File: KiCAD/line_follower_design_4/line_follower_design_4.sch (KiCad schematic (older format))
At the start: 50 parts

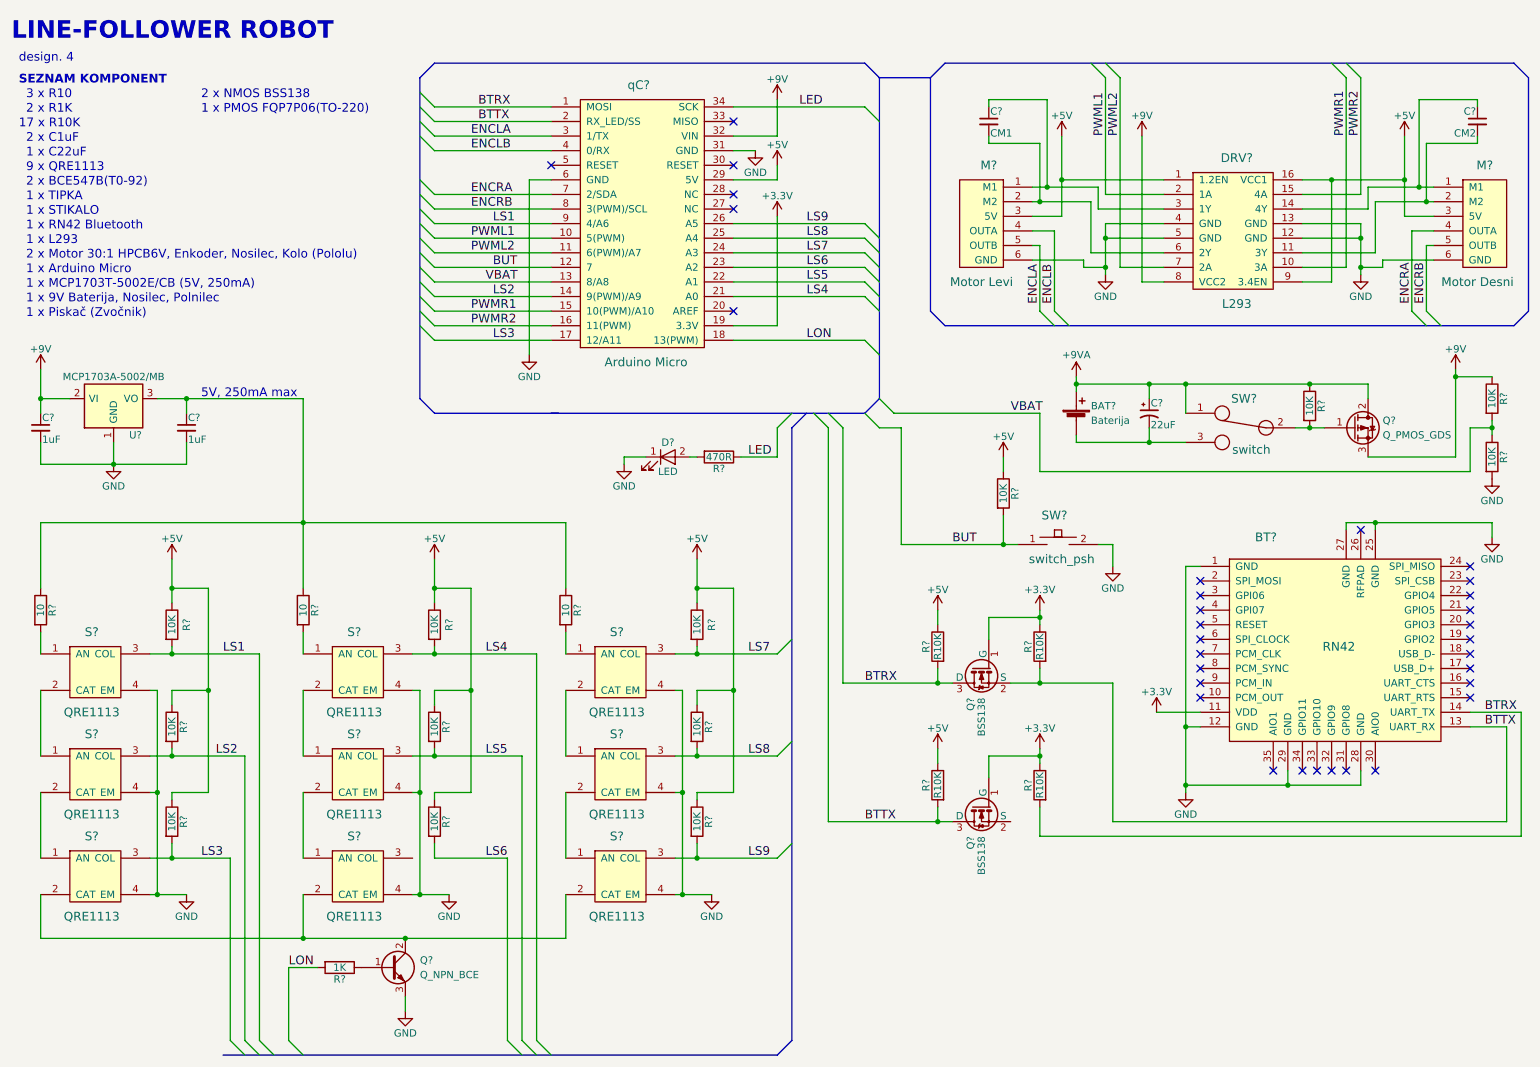
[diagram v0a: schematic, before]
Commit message: line-follower-design 4 updates
Shematic updates, library updates, netlist, unrouted PCB layout (1st
iteration).
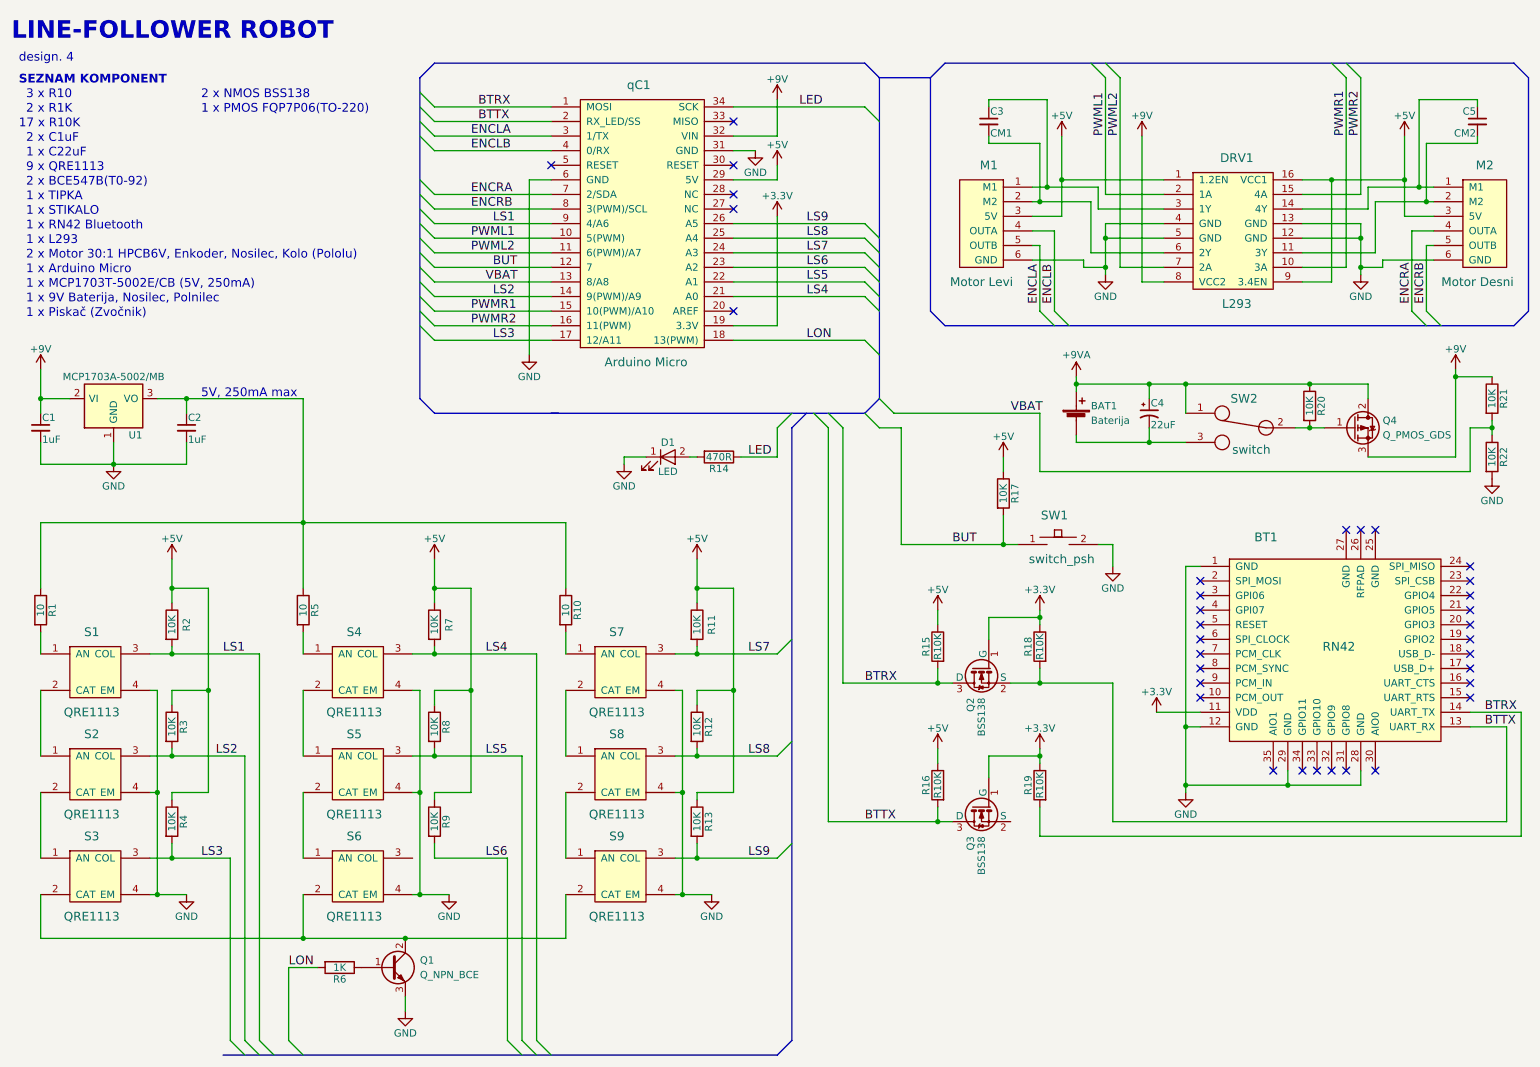
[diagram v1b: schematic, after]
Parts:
- BAT1: renamed from BAT?; footprint (none) -> 9VBattery_holder:12BH611-GR
- BT1: renamed from BT?; footprint (none) -> RF_Modules:RN42
- C1, C2, C3, C4, C5: renamed from C?; footprint (none) -> Capacitors_SMD:C_0603_HandSoldering
- D1: renamed from D?; footprint (none) -> LEDs:LED_D3.0mm_Horizontal_O1.27mm_Z2.0mm
- DRV1: renamed from DRV?; footprint (none) -> L293D:L293D
- M1, M2: renamed from M?; footprint (none) -> HPCBMotor:HPCB Motor (Pololu)
- Q1: renamed from Q?; footprint (none) -> Transistors_OldSowjetAera:OldSowjetaera_Transistor_Type-I_SmallPads
- Q4: renamed from Q?; footprint (none) -> TO_SOT_Packages_THT:TO-220_Horizontal
- R1, R10, R11, R12, R13, R14, R15, R16, R17, R18, R19, R2, R20, R21, R22, R3, R4, R5, R6, R7, R8, R9: renamed from R?; footprint (none) -> Resistors_SMD:R_1210_HandSoldering
- S1, S2, S3, S4, S5, S6, S7, S8, S9: renamed from S?; footprint (none) -> QRE1113:QRE1113
- SW1: renamed from SW?; footprint (none) -> Buttons_Switches_SMD:SW_SPST_EVQP0
- SW2: renamed from SW?; footprint (none) -> Buttons_Switches_SMD:SW_SPST_B3U-3100P
- gave numbers to parts that had none: 4
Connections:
- net GND: no longer BT1.25 (GND), BT1.27 (GND)
- no-connect marks 32 -> 34

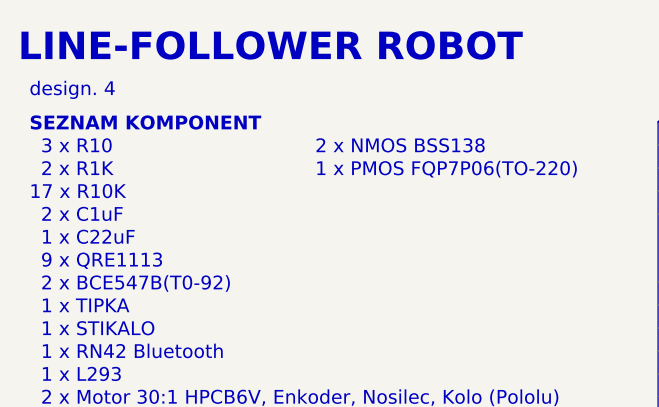
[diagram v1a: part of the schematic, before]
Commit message: line-follower-design-4 schematic update, pcb update
Library dependencies update, PCB components optimizations.
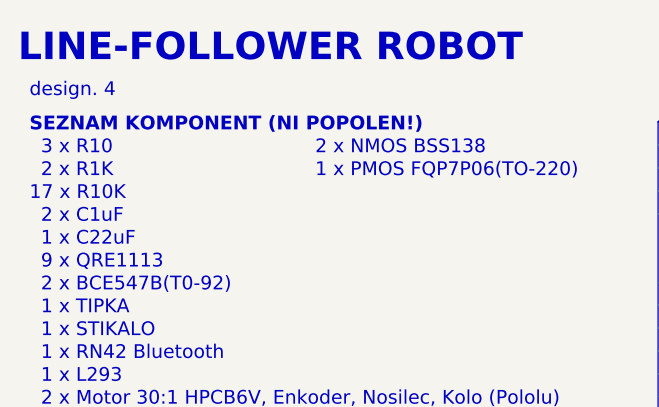
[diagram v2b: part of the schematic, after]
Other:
- note added: "SEZNAM KOMPONENT (NI POPOLEN!)\n"
- note removed: "SEZNAM KOMPONENT\n"
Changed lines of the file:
@@
 	6000 3400 6100 3300
 Text Notes 700  1050 0    60   ~ 12
-SEZNAM KOMPONENT\n
+SEZNAM KOMPONENT (NI POPOLEN!)\n
 Text Notes 750  1150 0    60   ~ 0
 3 x R10
